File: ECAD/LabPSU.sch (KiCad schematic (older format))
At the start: 45 parts, among them J1 PWR

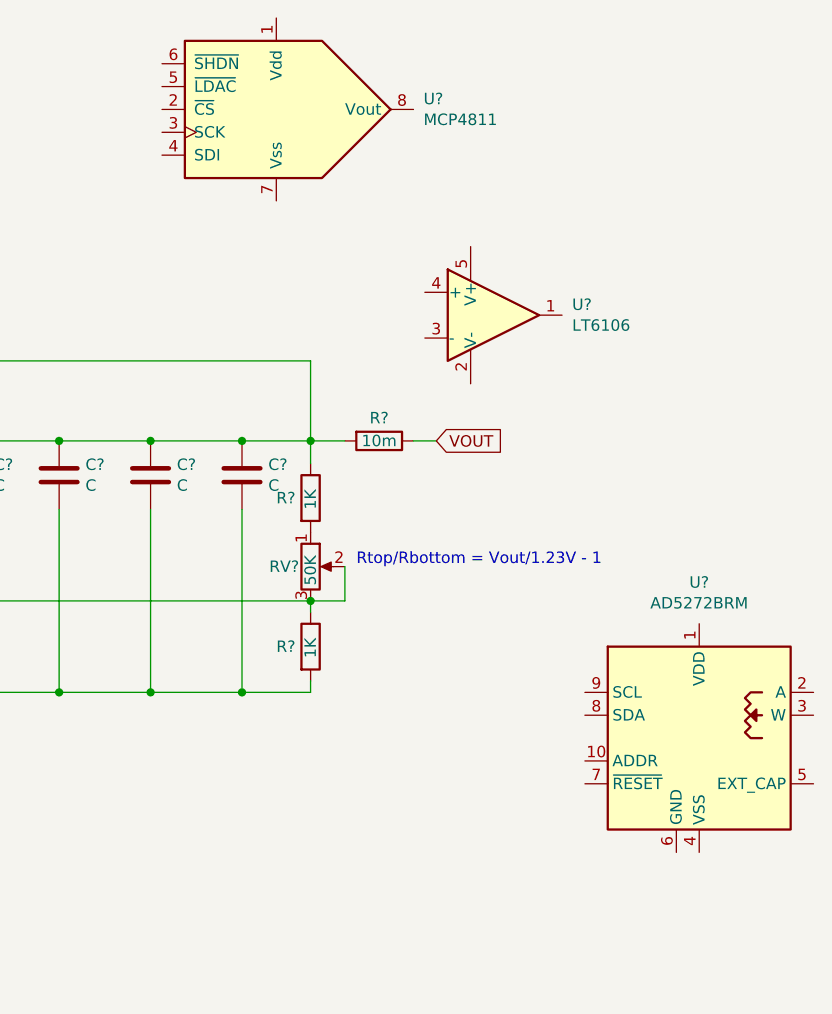
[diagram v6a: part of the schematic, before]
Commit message: Use dual gang pot instead of digital control
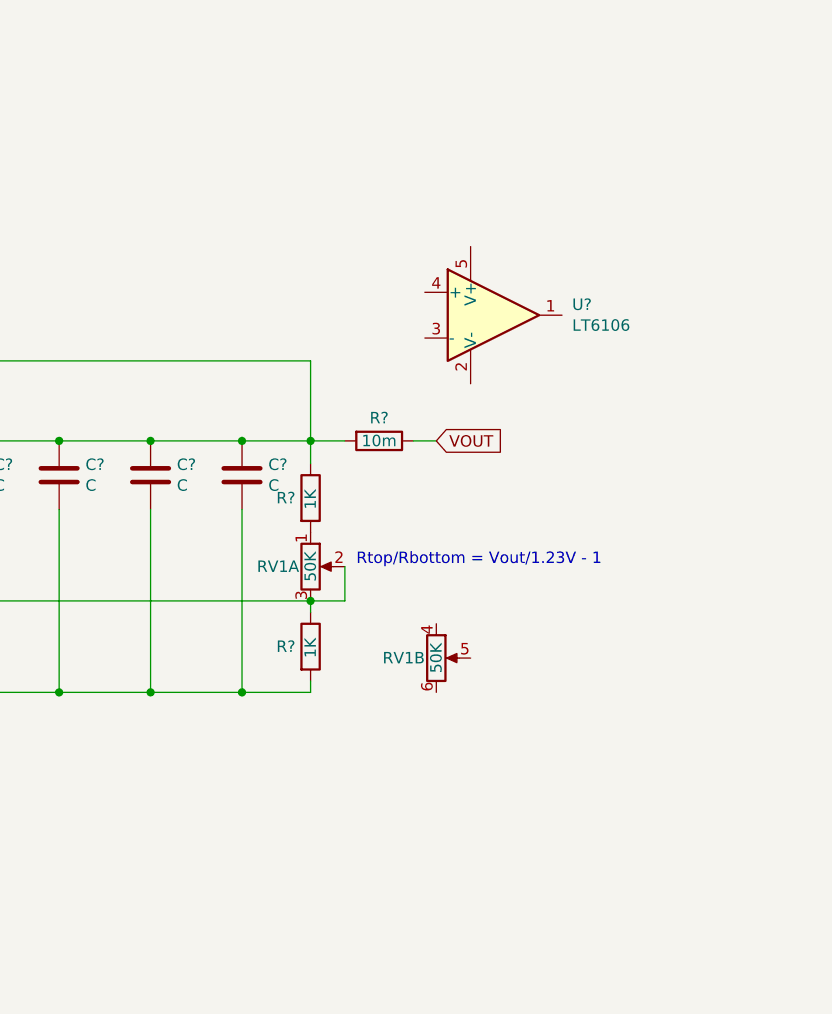
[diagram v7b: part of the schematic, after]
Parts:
- removed RV?: 50K, symbol Device:R_POT
- removed U?: AD5272BRM, Package_SO:MSOP-10_3x3mm_P0.5mm, symbol Potentiometer_Digital:AD5272BRM
- removed U?: MCP4811, symbol Analog_DAC:MCP4811
- added RV1: 50K, symbol Device:R_POT_Dual_Separate
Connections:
- net at C?.1, R?.1, R?.2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: now also RV1.2, RV1.3
- net at R?.2: now also RV1.1
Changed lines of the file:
@@
 Wire Wire Line
 	9700 3400 9700 3550
-$Comp
-L Device:R_POT RV?
-U 1 1 61C94316
-P 9550 3400
-F 0 "RV?" H 9500 3400 50  0000 R CNN
-F 1 "50K" V 9550 3450 50  0000 R CNN
-F 2 "" H 9550 3400 50  0001 C CNN
-F 3 "~" H 9550 3400 50  0001 C CNN
-	1    9550 3400
-	1    0    0    -1
-$EndComp
 Wire Wire Line
 	6050 2950 7050 2950
@@
 $EndComp
 $Comp
-L Potentiometer_Digital:AD5272BRM U?
-U 1 1 61C321DA
-P 11250 4150
-F 0 "U?" H 11250 4831 50  0000 C CNN
-F 1 "AD5272BRM" H 11250 4740 50  0000 C CNN
-F 2 "Package_SO:MSOP-10_3x3mm_P0.5mm" H 12000 3700 50  0001 C CNN
-F 3 "https://www.analog.com/media/en/technical-documentation/data-sheets/AD5272_5274.pdf" H 11250 4150 50  0001 C CNN
-	1    11250 4150
-	1    0    0    -1
-$EndComp
-$Comp
-L Analog_DAC:MCP4811 U?
-U 1 1 61C336A7
-P 9400 1400
-F 0 "U?" H 10044 1446 50  0000 L CNN
-F 1 "MCP4811" H 10044 1355 50  0000 L CNN
-F 2 "" H 10300 1300 50  0001 C CNN
-F 3 "http://ww1.microchip.com/downloads/en/DeviceDoc/22244B.pdf" H 10300 1300 50  0001 C CNN
-	1    9400 1400
-	1    0    0    -1
-$EndComp
+L Device:R_POT_Dual_Separate RV1
+U 1 1 61D78DDD
+P 9550 3400
+F 0 "RV1" H 9500 3400 50  0000 R CNN
+F 1 "50K" V 9550 3400 50  0000 C CNN
+F 2 "" H 9550 3400 50  0001 C CNN
+F 3 "~" H 9550 3400 50  0001 C CNN
+	1    9550 3400
+	1    0    0    -1
+$EndComp
+$Comp
+L Device:R_POT_Dual_Separate RV1
+U 2 1 61D795D0
+P 10100 3800
+F 0 "RV1" H 10050 3800 50  0000 R CNN
+F 1 "50K" V 10100 3800 50  0000 C CNN
+F 2 "" H 10100 3800 50  0001 C CNN
+F 3 "~" H 10100 3800 50  0001 C CNN
+	2    10100 3800
+	1    0    0    -1
+$EndComp

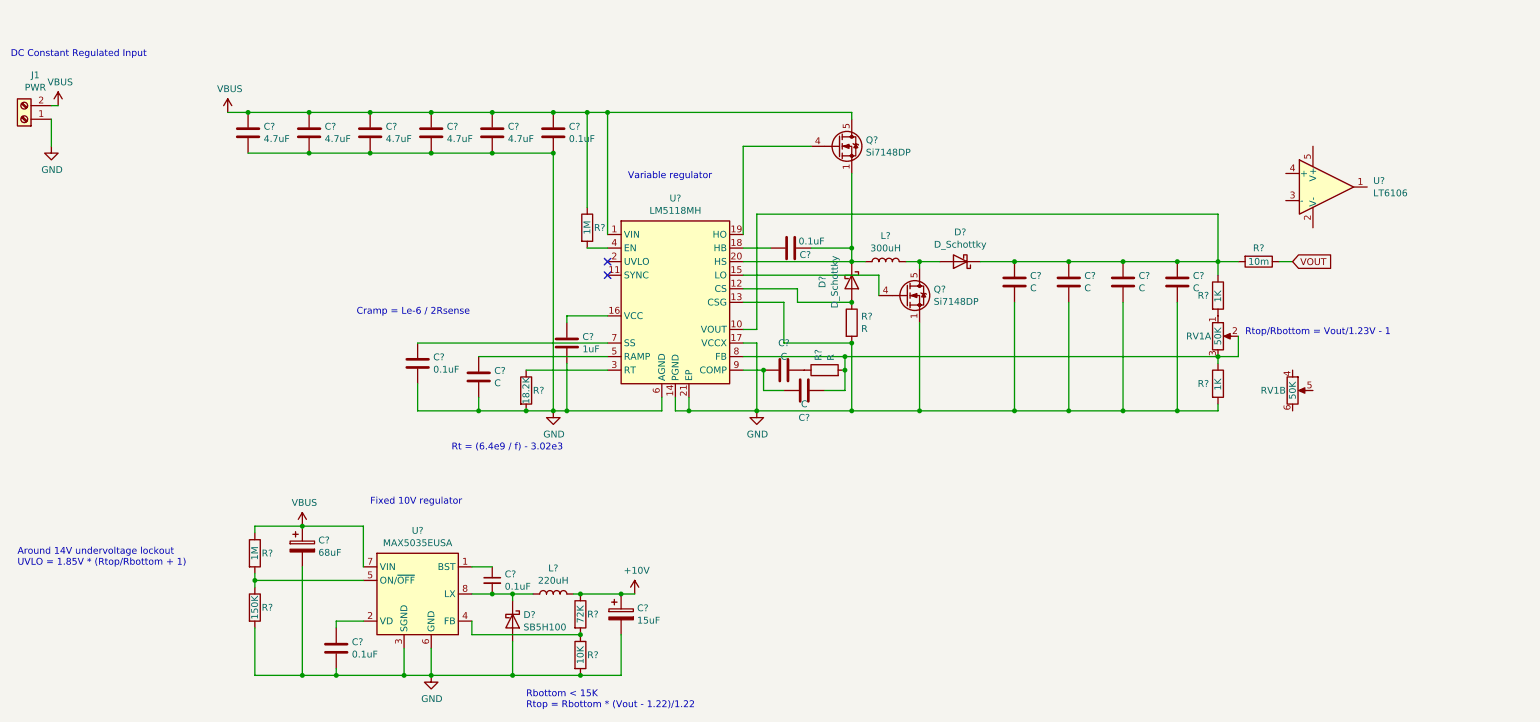
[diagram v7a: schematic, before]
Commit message: revamp current control for analog control
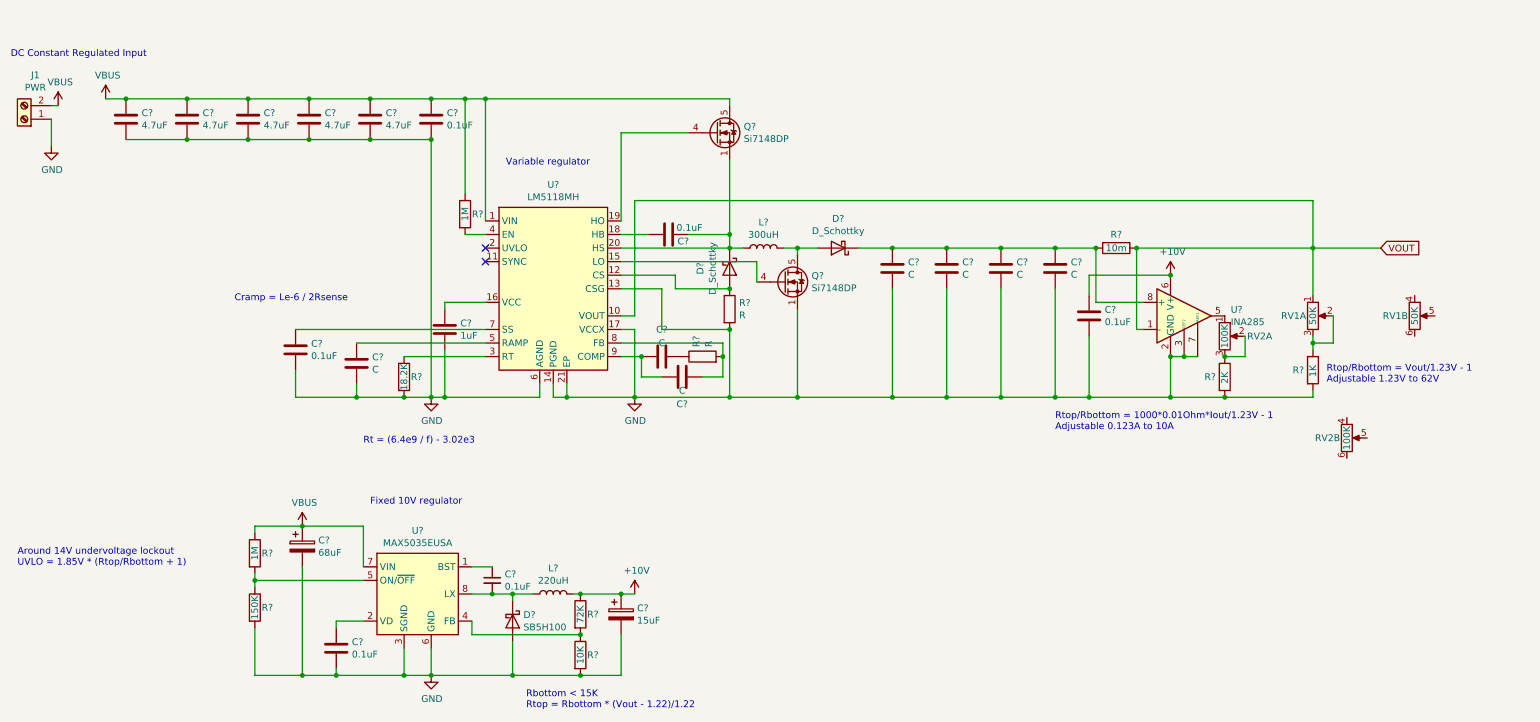
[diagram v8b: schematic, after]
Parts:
- removed R?: 1K, symbol Device:R
- removed U?: LT6106, Package_TO_SOT_SMD:SOT-23-5, symbol Amplifier_Current:LT6106
- added C?: 0.1uF, symbol Device:C
- added R?: 2K, symbol Device:R
- added RV2: 100K, symbol Device:R_POT_Dual_Separate
- added U?: INA285, symbol Amplifier_Current:INA285
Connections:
- net +10V: now also C?.1, U?.6 (V+)
- net GND: now also C?.2, R?.2, U?.2 (GND), U?.3 (REF2), U?.7 (REF1)
- net VOUT: now also RV1.1, U?.10 (VOUT), U?.1 (-)
- net at C?.1, C?.1, C?.1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: now also U?.8 (+); no longer U?.10 (VOUT)
- net at C?.1, R?.2, U?.8 (FB): no longer R?.1, RV1.2, RV1.3
- new net: R?.1, RV1.2, RV1.3
- new net: RV2.1, U?.5
- new net: R?.1, RV2.2, RV2.3
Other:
- note added: "Rtop/Rbottom = 1000*0.01Ohm*Iout/1.23V - 1\nAdjustable 0.123A to 10A"
- note added: "Rtop/Rbottom = Vout/1.23V - 1\nAdjustable 1.23V to 62V"
- note removed: "Rtop/Rbottom = Vout/1.23V - 1"
- moved on the sheet: C?, D?, L?, Q?, R?, RV1A, RV1B, U?
